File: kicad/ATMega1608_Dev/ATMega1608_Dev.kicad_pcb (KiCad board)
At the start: 2 copper layers, 50.8 x 25.4 mm, 0 parts

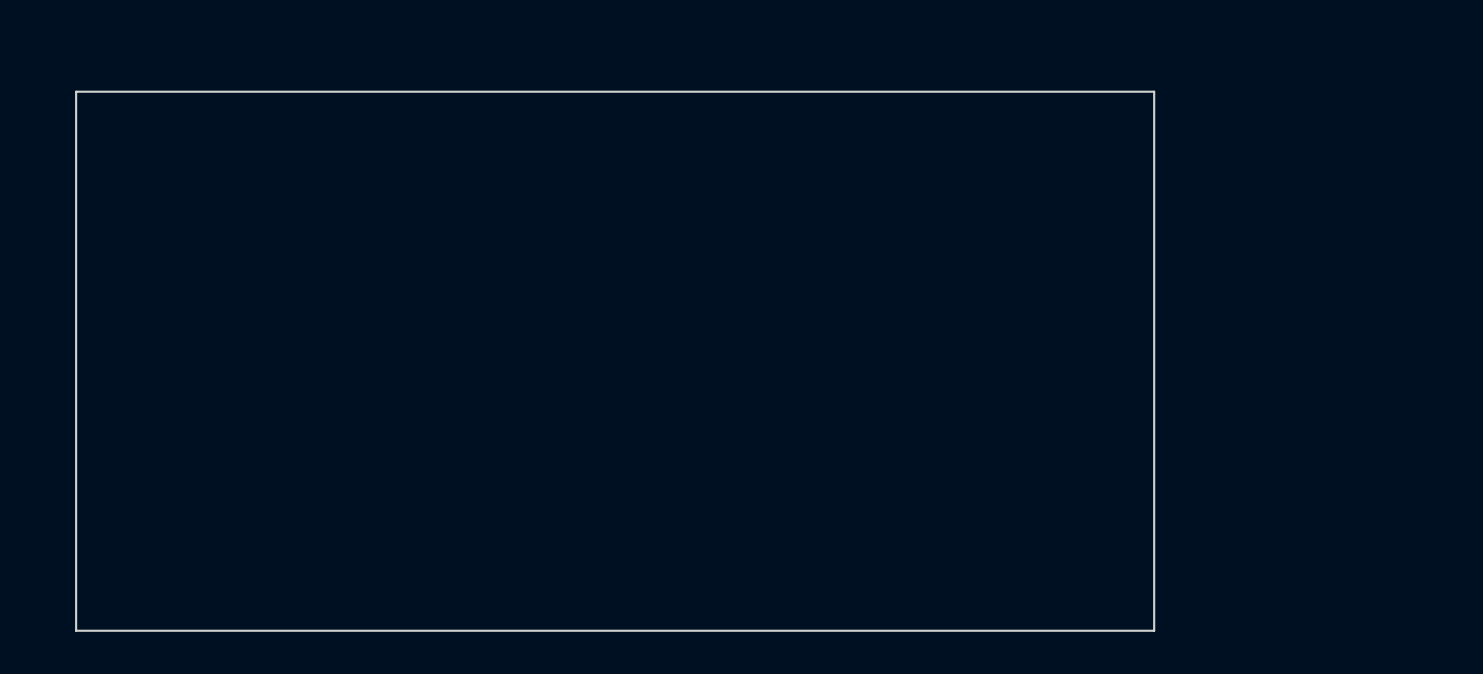
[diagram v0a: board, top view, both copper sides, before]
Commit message: Started on the layout
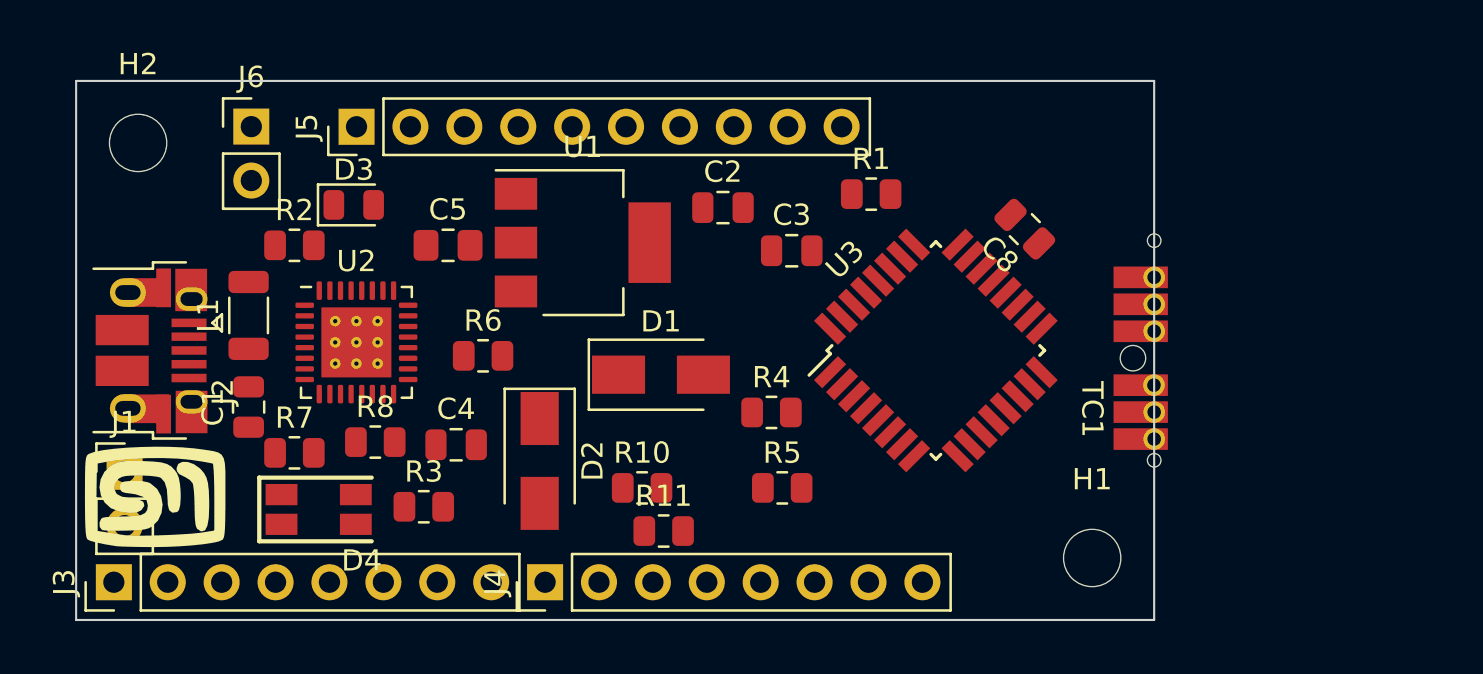
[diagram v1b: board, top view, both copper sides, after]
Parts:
- added C1: 10nF, Capacitor_SMD:C_0805_2012Metric, F.Cu at (119.9, 65.7)
- added C2: 100nF, Capacitor_SMD:C_0805_2012Metric, F.Cu at (142.2, 56.3)
- added C3: 4.7μF, Capacitor_SMD:C_0805_2012Metric, F.Cu at (145.5, 58.3)
- added C4: 4.7μF, Capacitor_SMD:C_0805_2012Metric, F.Cu at (129.7, 67.4)
- added C5: 1μF, Capacitor_SMD:C_0805_2012Metric_Pad1.18x1.45mm_HandSolder, F.Cu at (129.3, 58.0)
- added C8: 100nF, Capacitor_SMD:C_0805_2012Metric, F.Cu at (156.5, 57.3)
- added D1: B130-13-F, Diode_SMD:D_SMA, F.Cu at (139.3, 64.1)
- added D2: B130-13-F, Diode_SMD:D_SMA, F.Cu at (133.6, 68.2)
- added D3: LED, LED_SMD:LED_0805_2012Metric, F.Cu at (124.8, 56.1)
- added D4: RED_GREEN, atmega1608_footprints:LED_KKAA_15-22SURSYGC, F.Cu at (123.2, 70.5)
- added H1: MountingHole, MountingHole:MountingHole_2.7mm_M2.5, F.Cu at (159.6, 72.8)
- added H2: MountingHole, MountingHole:MountingHole_2.7mm_M2.5, F.Cu at (114.7, 53.2)
- added J1: Alt Power, Connector_PinHeader_2.54mm:PinHeader_1x02_P2.54mm_Vertical, F.Cu at (114.0, 68.7)
- added J2: USB_B_Micro, Connector_USB:USB_Micro-B_Amphenol_10103594-0001LF_Horizontal, F.Cu at (115.3, 63.0)
- added J3: Comm, Connector_PinHeader_2.54mm:PinHeader_1x08_P2.54mm_Vertical, F.Cu at (113.5, 73.9)
- added J4: GPIO1, Connector_PinHeader_2.54mm:PinHeader_1x08_P2.54mm_Vertical, F.Cu at (133.9, 73.9)
- added J5: GPIO2, Connector_PinHeader_2.54mm:PinHeader_1x10_P2.54mm_Vertical, F.Cu at (125.0, 52.5)
- added J6: Power OUT, Connector_PinHeader_2.54mm:PinHeader_1x02_P2.54mm_Vertical, F.Cu at (120.0, 52.4)
- added L1: 33Ω, Inductor_SMD:L_1206_3216Metric, F.Cu at (119.9, 61.3)
- added LG1: logo, mech:MyBasic_rounded_50_1, B.Cu at (159.0, 52.8)
- added LG2: logo, mech:MyBasic_rounded_50_1, F.Cu at (115.4, 69.8)
- added LG3: logo, Symbol:KiCad-Logo_5mm_SilkScreen, B.Cu at (155.6, 69.3)
- added R1: 0Ω, Resistor_SMD:R_0805_2012Metric, F.Cu at (149.2, 55.6)
- added R10: 0Ω, Resistor_SMD:R_0805_2012Metric, F.Cu at (138.4, 69.5)
- added R11: 0Ω, Resistor_SMD:R_0805_2012Metric, F.Cu at (139.4, 71.5)
- added R2: 270Ω, Resistor_SMD:R_0805_2012Metric, F.Cu at (122.0, 58.0)
- added R3: 0Ω, Resistor_SMD:R_0805_2012Metric, F.Cu at (128.1, 70.4)
- added R4: 0Ω, Resistor_SMD:R_0805_2012Metric, F.Cu at (144.5, 65.9)
- added R5: NOPOP, Resistor_SMD:R_0805_2012Metric, F.Cu at (145.0, 69.5)
- added R6: NOPOP, Resistor_SMD:R_0805_2012Metric, F.Cu at (130.9, 63.2)
- added R7: 270Ω, Resistor_SMD:R_0805_2012Metric, F.Cu at (122.0, 67.8)
- added R8: 270Ω, Resistor_SMD:R_0805_2012Metric, F.Cu at (125.9, 67.3)
- added TC1: ISP, atmega1608_footprints:Tag-Connect EC06, F.Cu at (162.6, 63.4)
- added U1: TC1262-33, Package_TO_SOT_SMD:SOT-223-3_TabPin2, F.Cu at (135.6, 57.9)
- added U2: FT232RQ, Package_DFN_QFN:QFN-32-1EP_5x5mm_P0.5mm_EP3.3x3.3mm_ThermalVias, F.Cu at (125.0, 62.6)
- added U3: ATMega1608_32, Package_QFP:TQFP-32_7x7mm_P0.8mm, F.Cu at (152.3, 63.0)

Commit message: The layout is complete - pending verification of USB interface
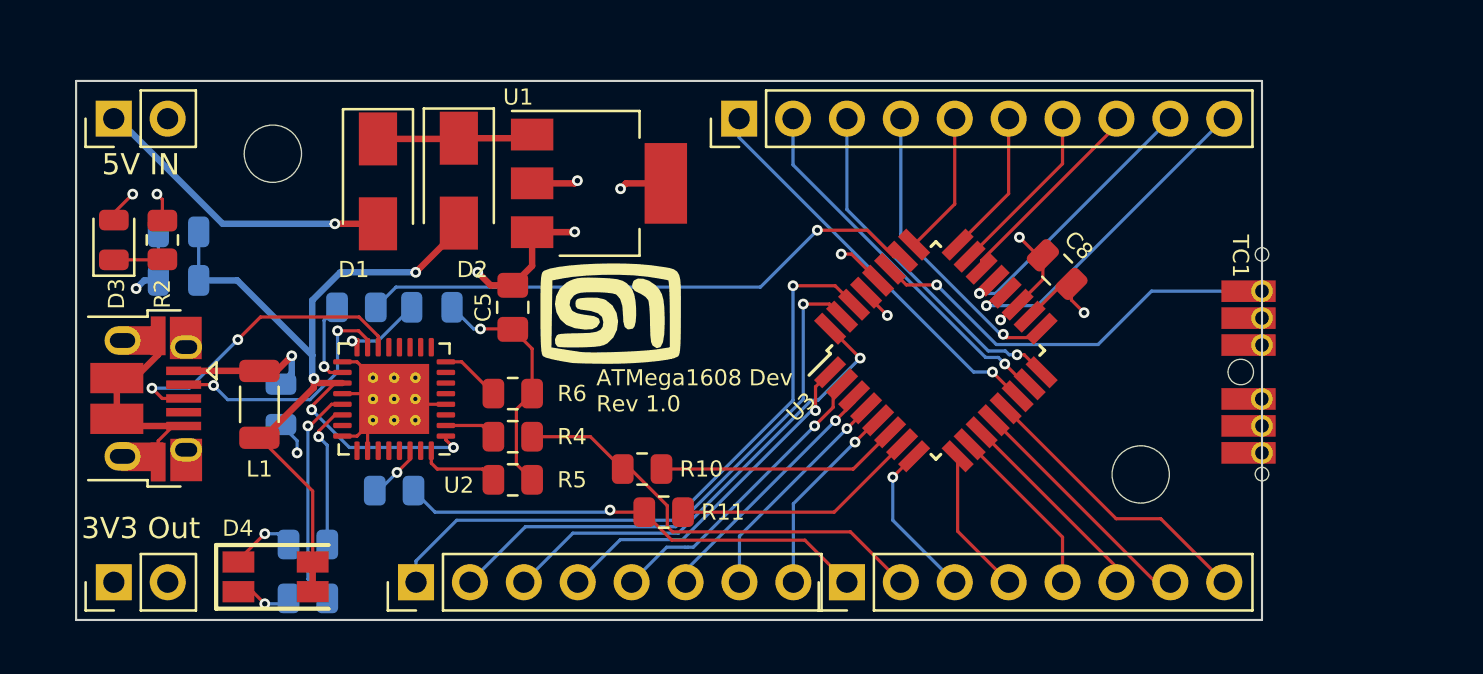
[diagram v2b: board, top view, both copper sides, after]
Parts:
- C1, C2, C3, C4, R1, R3, R7, R8: moved to B.Cu
- moved C3 28.9 mm to (116.6, 59.7), turned to 180 degrees
- moved C2 25.7 mm to (116.6, 57.4), turned to 180 degrees
- moved R1 24.8 mm to (125.0, 61.0), turned to 180 degrees
- moved LG2 23.1 mm to (136.9, 61.2)
- moved J6 22.4 mm to (113.5, 73.9), turned to 90 degrees
- moved J5 18.0 mm to (143.0, 52.1)
- moved J1 16.6 mm to (113.5, 52.1), turned to 90 degrees
- moved D1 16.2 mm to (126.0, 55.0), turned to -90 degrees
- moved J3 14.2 mm to (127.8, 73.9)
- moved J4 14.2 mm to (148.1, 73.9)
- moved D2 13.7 mm to (129.8, 55.0)
- moved R5 12.7 mm to (132.3, 69.1)
- moved R4 12.2 mm to (132.3, 67.1)
- moved D3 11.4 mm to (113.5, 57.8), turned to 90 degrees
- moved R8 8.02 mm to (122.7, 74.7)
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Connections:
- J3 pad 1: /SDA -> /TxD0
- J3 pad 2: /SCL -> /RxD0
- J3 pad 3: /TxD0 -> /SDA
- J3 pad 4: /RxD0 -> /SCL
- J4 pad 1: /DOUT -> /DIN
- J4 pad 2: /DIN -> /DOUT
- J5 pad 10: /PF5 -> /PF0
- J5 pad 5: /PF0 -> /PF5
- J5 pad 6: /PF1 -> /PF4
- J5 pad 7: /PF2 -> /PF3
- J5 pad 8: /PF3 -> /PF2
- J5 pad 9: /PF4 -> /PF1
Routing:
- net GND: track 0.00 -> 48.3 mm, vias 0 -> 9
- net Net-(C2-Pad1): track 0.00 -> 45.3 mm, vias 0 -> 4
- net /TxD0: track 0.00 -> 30.5 mm, vias 0 -> 1
- net /~{RESET}: track 0.00 -> 26.8 mm, vias 0 -> 1
- net /RxD0: track 0.00 -> 25.8 mm, vias 0 -> 1
- net /DIN: track 0.00 -> 22.3 mm, vias 0 -> 1
- net /SDA: track 0.00 -> 22.2 mm, vias 0 -> 1
- net /DOUT: track 0.00 -> 20.8 mm
- net /UPDI: track 0.00 -> 20.0 mm, vias 0 -> 1
- net /PD4: track 0.00 -> 19.1 mm, vias 0 -> 1
- net /PD5: track 0.00 -> 17.6 mm, vias 0 -> 1
- net /SCL: track 0.00 -> 16.6 mm, vias 0 -> 1
- net /PD6: track 0.00 -> 16.6 mm, vias 0 -> 1
- net /PF0: track 0.00 -> 16.0 mm, vias 0 -> 1
- net +3V3: track 0.00 -> 14.9 mm, vias 0 -> 5
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- added copper zone on In2.Cu, net +3V3
- added copper zone on In1.Cu, net GND
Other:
- board size 50.8 x 25.4 mm -> 55.9 x 25.4 mm
- copper layers 2 -> 4
- board text added: "ATMega1608 Dev Rev 1.0"

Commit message: Fixes some labeling issues
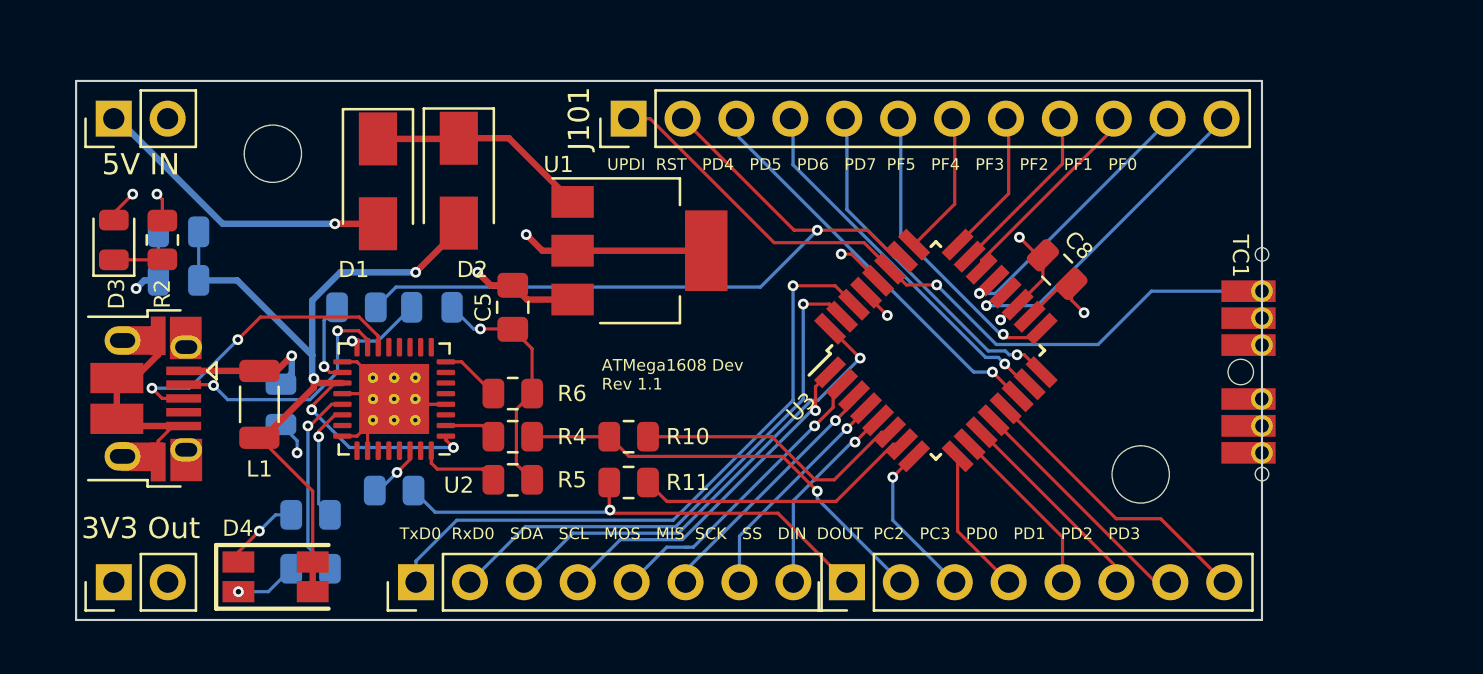
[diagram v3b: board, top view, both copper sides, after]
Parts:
- removed J5: GPIO2, Connector_PinHeader_2.54mm:PinHeader_1x10_P2.54mm_Vertical
- removed LG2: logo, mech:MyBasic_rounded_50_1
- added J101: GPIO2, Connector_PinHeader_2.54mm:PinHeader_1x12_P2.54mm_Vertical, F.Cu at (137.8, 52.1)
- moved U1 3.70 mm to (138.3, 58.3)
- moved R11 2.16 mm to (137.8, 69.2)
- moved R10 1.65 mm to (137.8, 67.1)
- moved R8 1.40 mm to (122.8, 73.3)
- moved R7 1.40 mm to (122.8, 70.7)
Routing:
- net /UPDI: track 20.0 -> 35.2 mm
- net /~{RESET}: track 26.8 -> 35.4 mm
- net GND: track 48.3 -> 52.6 mm, vias 9 -> 8
- net +5V: track 7.35 -> 10.4 mm
- net Net-(R11-Pad1): track 11.6 -> 13.5 mm
- net +3V3: track 14.9 -> 13.1 mm, vias 5 -> 4
- net Net-(R10-Pad1): track 11.5 -> 13.2 mm
- net Net-(R8-Pad2): track 10.6 -> 9.21 mm
- net Net-(R7-Pad2): track 6.94 -> 5.60 mm
- net /DIN: track 22.3 -> 23.6 mm
- net Net-(D4-Pad2): track 3.18 -> 3.68 mm
- net /DOUT: track 20.8 -> 20.4 mm, vias 0 -> 1
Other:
- board text added: "ATMega1608 Dev Rev 1.1"
- board text added: "TxD0 RxD0 SDA SCL MOS MIS SCK SS DIN DOUT PC2 PC3 PD0 PD1 PD2 PD3"
- board text added: "UPDI RST PD4 PD5 PD6 PD7 PF5 PF4 PF3 PF2 PF1 PF0"
- board text removed: "ATMega1608 Dev Rev 1.0"

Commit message: Moved the USART_Troubleshooting changes to main
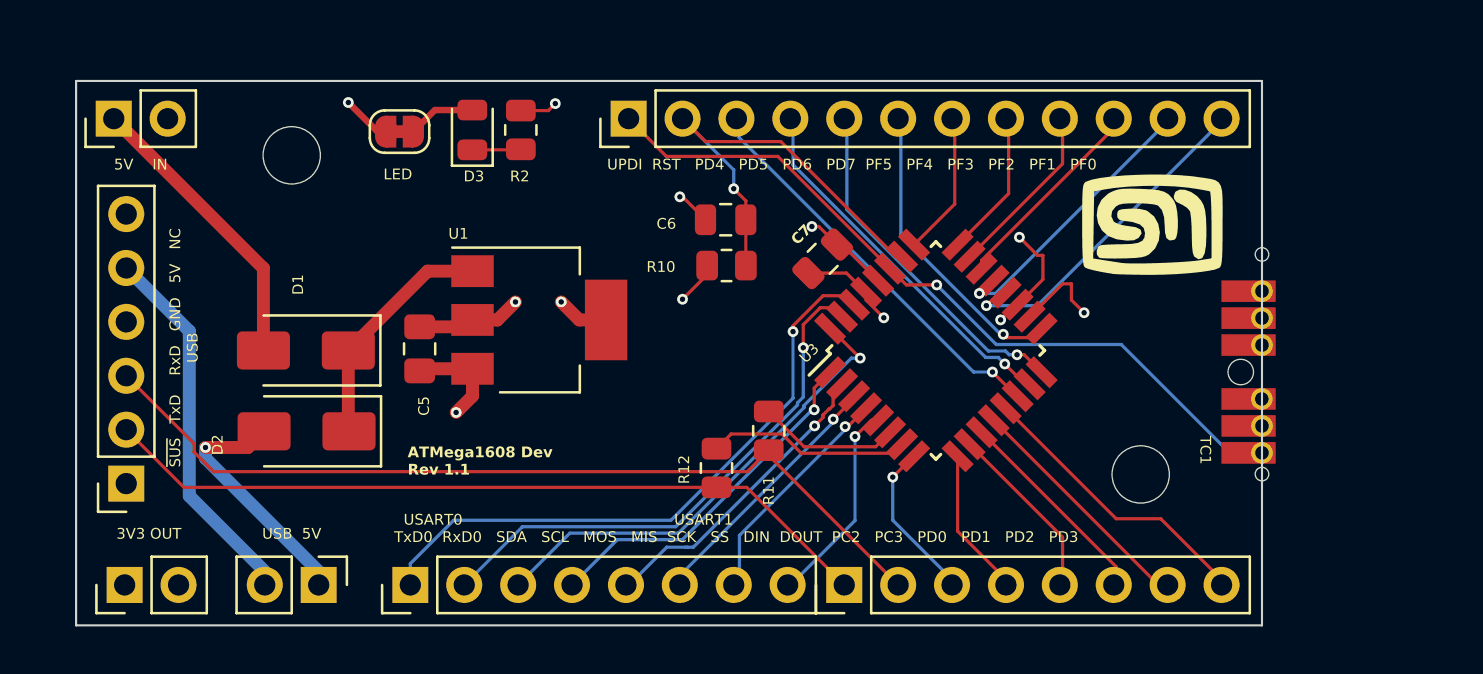
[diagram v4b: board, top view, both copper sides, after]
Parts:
- removed C1: 10nF, Capacitor_SMD:C_0805_2012Metric
- removed C2, C8: 100nF, Capacitor_SMD:C_0805_2012Metric
- removed C3, C4: 4.7μF, Capacitor_SMD:C_0805_2012Metric
- removed D4: RED_GREEN, atmega1608_footprints:LED_KKAA_15-22SURSYGC
- removed J101: GPIO2, Connector_PinHeader_2.54mm:PinHeader_1x12_P2.54mm_Vertical
- removed L1: 33Ω, Inductor_SMD:L_1206_3216Metric
- removed LG3: logo, Symbol:KiCad-Logo_5mm_SilkScreen
- removed R1, R3, R4: 0Ω, Resistor_SMD:R_0805_2012Metric
- removed R5, R6: NOPOP, Resistor_SMD:R_0805_2012Metric
- removed R7, R8: 270Ω, Resistor_SMD:R_0805_2012Metric
- removed U2: FT232RQ, Package_DFN_QFN:QFN-32-1EP_5x5mm_P0.5mm_EP3.3x3.3mm_ThermalVias
- added C6: 100nF, Capacitor_SMD:C_0805_2012Metric, F.Cu at (142.4, 56.8)
- added C7: 100nF, Capacitor_SMD:C_0805_2012Metric, F.Cu at (146.9, 58.7)
- added J5: GPIO2, Connector_PinHeader_2.54mm:PinHeader_1x12_P2.54mm_Vertical, F.Cu at (137.8, 52.1)
- added JP101: USB Pwr, Connector_PinHeader_2.54mm:PinHeader_1x02_P2.54mm_Vertical, F.Cu at (123.2, 74.0)
- added JP102: Indicator LED, Jumper:SolderJumper-2_P1.3mm_Bridged_RoundedPad1.0x1.5mm, F.Cu at (127.0, 52.7)
- added LG2: logo, Symbol:KiCad-Logo_5mm_SilkScreen, B.Cu at (157.9, 59.6)
- added R12: 0Ω, Resistor_SMD:R_0805_2012Metric, F.Cu at (141.9, 68.5)
- J2: value USB_B_Micro -> USART-USB; footprint Connector_USB:USB_Micro-B_Amphenol_10103594-0001LF_Horizontal -> Connector_PinSocket_2.54mm:PinSocket_1x06_P2.54mm_Vertical
- J3: value Comm -> GPIO1
- J4: value GPIO1 -> Power OUT; footprint Connector_PinHeader_2.54mm:PinHeader_1x08_P2.54mm_Vertical -> Connector_PinHeader_2.54mm:PinHeader_1x02_P2.54mm_Vertical
- J6: value Power OUT -> Comm; footprint Connector_PinHeader_2.54mm:PinHeader_1x02_P2.54mm_Vertical -> Connector_PinHeader_2.54mm:PinHeader_1x08_P2.54mm_Vertical
- LG1: moved to F.Cu
- R10: value 0Ω -> 10kΩ
- moved J4 34.0 mm to (114.0, 74.0)
- moved J3 20.2 mm to (148.0, 74.0)
- moved D3 17.7 mm to (130.4, 52.6)
- moved R2 17.7 mm to (132.7, 52.6)
- moved J6 14.0 mm to (127.5, 74.0)
- moved D2 13.8 mm to (122.6, 66.8), turned to 180 degrees
- moved R10 9.29 mm to (142.4, 59.0)
- moved D1 8.66 mm to (122.6, 63.0), turned to 180 degrees
- moved R11 7.04 mm to (144.4, 66.8), turned to -90 degrees
- moved U1 5.74 mm to (133.6, 61.6)
- moved C5 4.80 mm to (127.9, 62.9), turned to 90 degrees
- moved J2 4.10 mm to (114.1, 69.3), turned to 180 degrees
- moved LG1 1.25 mm to (162.4, 57.0), turned to 0 degrees
- moved H2 0.89 mm to (121.9, 53.8)
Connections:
- C5 pad 1: +3V3 -> +3.3V
- D2 pad 2: Net-(C2-Pad1) -> /USB-5V
- D3 pad 2: +3V3 -> Net-(D3-A)
- J2 pad 1: Net-(C1-Pad1) -> unconnected-(J2-Pin_1-Pad1)
- J2 pad 2: Net-(J2-Pad2) -> /DIN
- J2 pad 3: Net-(J2-Pad3) -> /DOUT
- J2 pad 4: unconnected-(J2-Pad4) -> GND
- J2 pad 5: GND -> Net-(J2-Pin_5)
- J2 pad 6: GND -> unconnected-(J2-Pin_6-Pad6)
- J3 pad 1: /TxD0 -> /DIN
- J3 pad 2: /RxD0 -> /DOUT
- J3 pad 3: /SDA -> /PC2
- J3 pad 4: /SCL -> /PC3
- J3 pad 5: /MOSI -> /PD0
- J3 pad 6: /MISO -> /PD1
- J3 pad 7: /SCK -> /PD2
- J3 pad 8: /SS -> /PD3
- J4 pad 1: /DIN -> +3.3V
- J4 pad 2: /DOUT -> GND
- J6 pad 1: +3V3 -> /TxD0
- J6 pad 2: GND -> /RxD0
- R10 pad 1: Net-(R10-Pad1) -> /~{RESET}
- R10 pad 2: /DOUT -> +3.3V
- R11 pad 1: Net-(R11-Pad1) -> Net-(U3-PC0/TxD1/2-WO/1-IN0)
- R11 pad 2: /DIN -> /DOUT
- TC1 pad 2: +3V3 -> +3.3V
- U1 pad 3: +3V3 -> +3.3V
- U3 pad 18: +3V3 -> +3.3V
- U3 pad 28: +3V3 -> +3.3V
- U3 pad 6: Net-(R10-Pad1) -> Net-(U3-PC0/TxD1/2-WO/1-IN0)
- U3 pad 7: Net-(R11-Pad1) -> Net-(U3-PC1/RxD1-IN1)
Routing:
- net Net-(C2-Pad1): track 45.3 -> 0.00 mm, vias 4 -> 0
- net GND: track 52.6 -> 20.9 mm, vias 8 -> 7
- net /DOUT: track 20.4 -> 41.7 mm, vias 1 -> 0
- net +3.3V: track 0.00 -> 17.7 mm, vias 0 -> 5
- net Net-(J2-Pin_5): track 0.00 -> 17.0 mm
- net Net-(J2-Pad3): track 14.6 -> 0.00 mm, vias 2 -> 0
- net /~{RESET}: track 35.4 -> 21.2 mm
- net Net-(R11-Pad1): track 13.5 -> 0.00 mm
- net /DIN: track 23.6 -> 36.9 mm, vias 1 -> 0
- net Net-(R10-Pad1): track 13.2 -> 0.00 mm
- net +3V3: track 13.1 -> 0.00 mm, vias 4 -> 0
- net Net-(J2-Pad2): track 12.0 -> 0.00 mm, vias 2 -> 0
- net /USB-5V: track 0.00 -> 11.1 mm, vias 0 -> 1
- net Net-(U3-PC1/RxD1-IN1): track 0.00 -> 9.58 mm
- net Net-(R8-Pad2): track 9.21 -> 0.00 mm, vias 1 -> 0
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- added copper zone on In2.Cu, net +3.3V
- removed copper zone on In2.Cu, net +3V3
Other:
- board size 55.9 x 25.4 mm -> 55.9 x 25.7 mm
- board text added: "LED"
- board text added: "USART0 USART1 TxD0 RxD0 SDA SCL MOS MIS SCK SS DIN DOUT PC2 PC3 PD0 PD1 PD2 PD3"
- board text added: "~{SUS} TxD RxD GND 5V NC USB"
- board text removed: "TxD0 RxD0 SDA SCL MOS MIS SCK SS DIN DOUT PC2 PC3 PD0 PD1 PD2 PD3"
